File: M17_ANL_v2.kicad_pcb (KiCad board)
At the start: 2 copper layers, 63.9 x 19.6 mm, 108 parts, among them IC1 ADF7021, J1 USB_A, J2 RF_PORT, J3 Conn_01x05, J4 Conn_01x05, U1 STM32F303CBTx, U2 AP1117-33, X1 ASV-xxxMHz, X2 ASV-xxxMHz

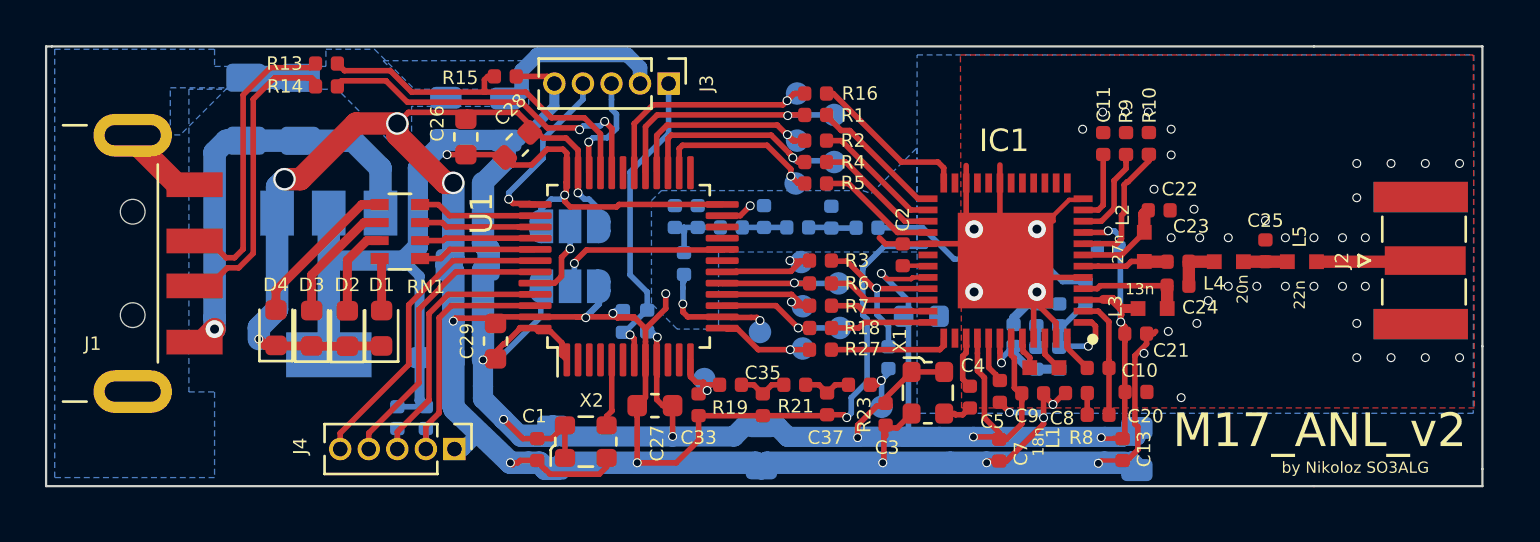
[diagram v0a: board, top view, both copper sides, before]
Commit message: added choke for radio part of M17_ANL_v2 added choke of input and output of the voltage regulator
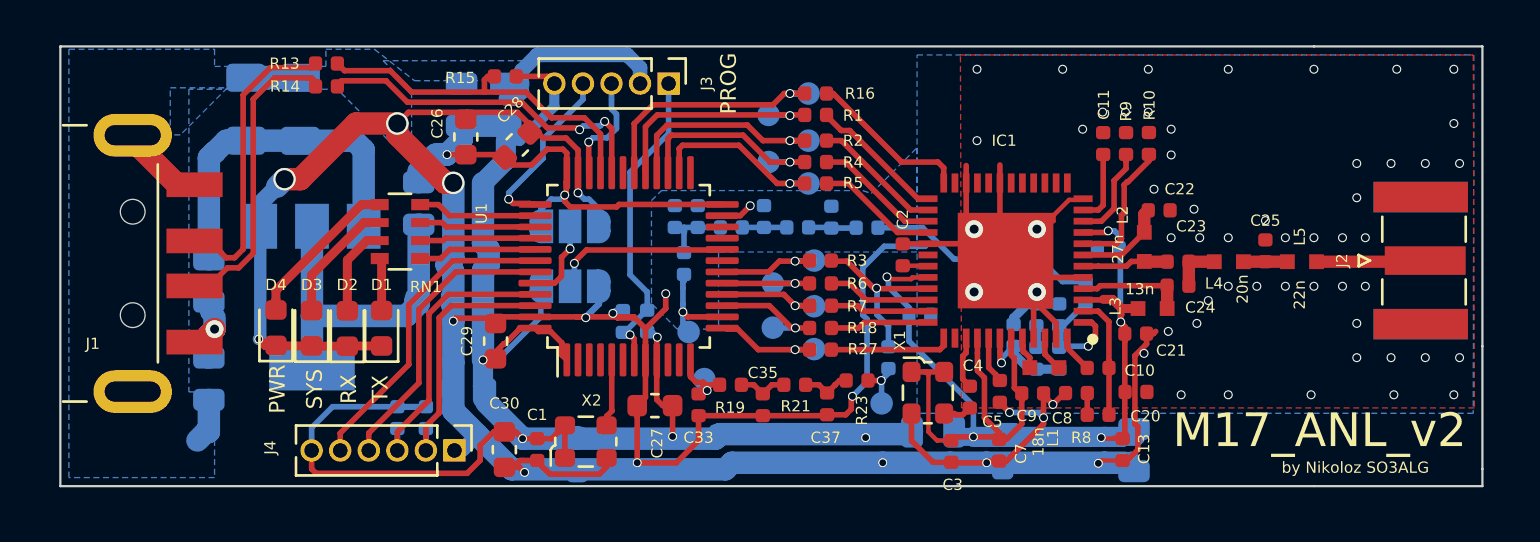
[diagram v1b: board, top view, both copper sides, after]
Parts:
- added C31: 10n, Capacitor_SMD:C_0402_1005Metric, B.Cu at (121.0, 98.2)
- added C44: 100n, Capacitor_SMD:C_0603_1608Metric, B.Cu at (99.4, 97.5)
- added C45: 100n, Capacitor_SMD:C_0805_2012Metric, B.Cu at (89.4, 101.0)
- added L6: 10uH, Inductor_SMD:L_0805_2012Metric, B.Cu at (98.7, 93.2)
- added L7: 1uH, Inductor_SMD:L_0805_2012Metric, B.Cu at (89.4, 96.6)
- added L8: 10uH, Inductor_SMD:L_0805_2012Metric, B.Cu at (121.6, 103.4)
- C30: moved to F.Cu
- C41, C42: value 10n -> 1n; footprint Capacitor_SMD:C_0805_2012Metric -> Capacitor_SMD:C_0603_1608Metric
- C43: value 10n -> 100n; footprint Capacitor_SMD:C_0805_2012Metric -> Capacitor_SMD:C_0603_1608Metric
- J3: value Conn_01x05 -> PROG
- J4: value Conn_01x05 -> Conn_01x06; footprint Connector_PinHeader_1.27mm:PinHeader_1x05_P1.27mm_Vertical -> Connector_PinHeader_1.27mm:PinHeader_1x06_P1.27mm_Vertical
- moved C31 16.5 mm to (105.8, 104.4), turned to 90 degrees
- moved C41 10.7 mm to (124.7, 104.3)
- moved C42 7.43 mm to (112.1, 104.3)
- moved C43 5.52 mm to (101.0, 101.5)
- moved C30 5.06 mm to (102.6, 104.2), turned to 90 degrees
- moved C3 3.36 mm to (122.4, 104.2)
- moved TP12 3.17 mm to (110.7, 98.9)
- moved TP9 2.98 mm to (114.5, 98.7)
- moved TP2 2.92 mm to (114.3, 91.4)
- moved TP4 2.92 mm to (114.3, 89.3)
- moved TP7 2.92 mm to (114.5, 96.8)
- moved U2 0.95 mm to (94.0, 97.4)
- moved C18 0.94 mm to (100.6, 88.8)
- moved C19 0.67 mm to (102.6, 88.8)
- moved TP8 0.58 mm to (116.3, 95.8)
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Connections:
- C1 pad 1: GND -> VCC_MCU
- C1 pad 2: MoDem_VCC -> GND
- C17 pad 1: VBUS -> Net-(C17-Pad1)
- C18 pad 1: MoDem_VCC -> VCC_MCU
- C19 pad 1: MoDem_VCC -> VCC_MCU
- C26 pad 2: MoDem_VCC -> VCC_MCU
- C27 pad 2: MoDem_VCC -> VCC_MCU
- C28 pad 1: MoDem_VCC -> VCC_MCU
- C29 pad 1: MoDem_VCC -> VCC_MCU
- C30 pad 2: MoDem_VCC -> VCC_MCU
- C31 pad 2: MoDem_VCC -> VCC_MCU
- C42 pad 1: MoDem_VCC -> VCC_MCU
- C43 pad 1: MoDem_VCC -> VCC_MCU
- C6 pad 1: VBUS -> Net-(C17-Pad1)
- J3 pad 5: MoDem_VCC -> VCC_MCU
- JP1 pad 1: MoDem_VCC -> VCC_MCU
- JP2 pad 1: MoDem_VCC -> VCC_MCU
- R15 pad 2: MoDem_VCC -> VCC_MCU
- R17 pad 2: MoDem_VCC -> VCC_MCU
- R28 pad 2: MoDem_VCC -> VCC_MCU
- R29 pad 2: MoDem_VCC -> VCC_MCU
- U1 pad 1: MoDem_VCC -> VCC_MCU
- U1 pad 24: MoDem_VCC -> VCC_MCU
- U1 pad 36: MoDem_VCC -> VCC_MCU
- U1 pad 48: MoDem_VCC -> VCC_MCU
- U1 pad 9: MoDem_VCC -> VCC_MCU
- U2 pad 2: MoDem_VCC -> Net-(C44-Pad1)
- U2 pad 3: VBUS -> Net-(C17-Pad1)
- X2 pad 1: MoDem_VCC -> VCC_MCU
- X2 pad 4: MoDem_VCC -> VCC_MCU
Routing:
- net MoDem_VCC: track 160.3 -> 53.8 mm, vias 12 -> 5
- net VCC_MCU: track 0.00 -> 102.3 mm, vias 0 -> 7
- net Net-(C17-Pad1): track 0.00 -> 15.3 mm
- net VBUS: track 19.1 -> 3.85 mm
- net Net-(C44-Pad1): track 0.00 -> 15.0 mm
- net GND: track 202.2 -> 205.7 mm, vias 60 -> 73
- net TxRx_Data: track 5.86 -> 4.88 mm
- net SPI_EN: track 11.5 -> 10.6 mm
- net DAC_OUT: track 5.79 -> 4.94 mm, vias 2 -> 1
- net SPI_MISO: track 10.4 -> 9.62 mm
- net RF_CLKOUT: track 6.03 -> 5.31 mm
- net SPI_MOSI: track 9.74 -> 9.14 mm
- net RF_EN: track 10.9 -> 11.4 mm
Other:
- board size 63.9 x 19.6 mm -> 63.2 x 19.6 mm
- board text added: "PWR"
- board text added: "RX"
- board text added: "SYS"
- board text added: "TX"

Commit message: Plotted new PDF of schematic
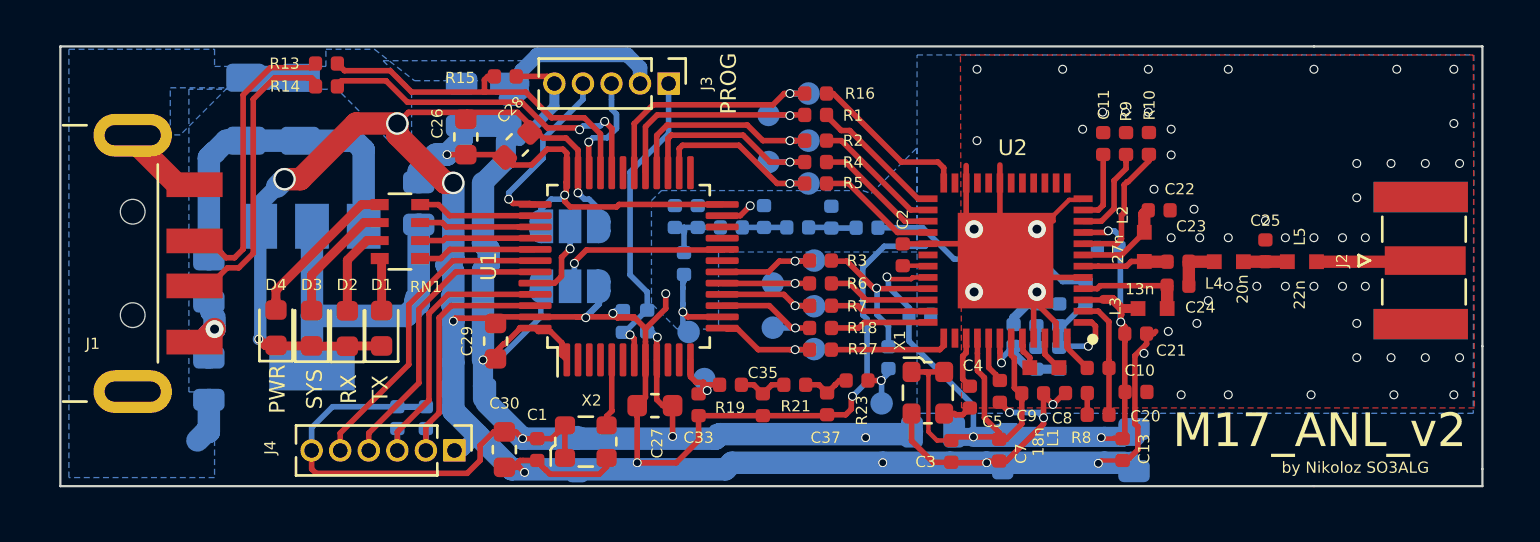
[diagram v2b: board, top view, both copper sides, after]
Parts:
- renumbered IC1 to U2, U2 to U3

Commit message: Readme header description added
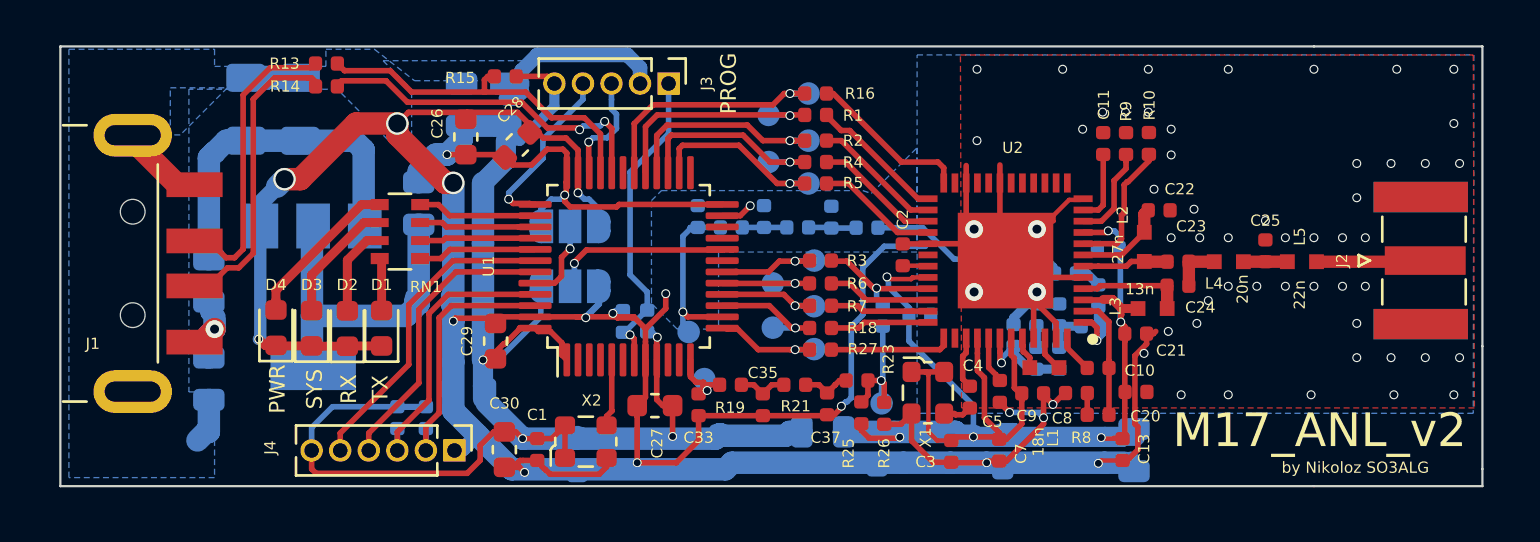
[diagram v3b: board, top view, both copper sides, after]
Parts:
- added C46: 1n, Capacitor_SMD:C_0603_1608Metric, B.Cu at (119.1, 104.1)
- added R31: 47k, Resistor_SMD:R_0402_1005Metric, B.Cu at (129.0, 97.3)
- added R32: 100, Resistor_SMD:R_0402_1005Metric, B.Cu at (128.7, 98.7)
- R24: value 1k -> 100k
- R25, R26: value ? -> 1k; moved to F.Cu
- moved R26 12.8 mm to (119.4, 102.6)
- moved R25 10.3 mm to (118.4, 102.5)
- moved L8 4.90 mm to (116.7, 103.4)
- moved C39 1.90 mm to (119.4, 98.2)
- moved C40 1.23 mm to (127.5, 96.3), turned to 180 degrees
- moved U3 0.05 mm to (94.0, 97.4)
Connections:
- C14 pad 1: VCO_IN -> Net-(C14-Pad1)
- C34 pad 2: Net-(C34-Pad2) -> DAC_OUT
- C40 pad 1: VCO_IN -> Net-(C40-Pad1)
- R11 pad 1: VCO_IN -> Net-(C14-Pad1)
- R20 pad 2: Net-(C34-Pad2) -> DAC_OUT
- R25 pad 1: Net-(C34-Pad2) -> FMDemod
- R25 pad 2: DAC_OUT -> MoDem_VCC
- R26 pad 1: Net-(C34-Pad2) -> GND
- R26 pad 2: GND -> FMDemod
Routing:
- net MoDem_VCC: track 53.8 -> 63.0 mm, vias 5 -> 6
- net VCC_MCU: track 102.3 -> 96.2 mm, vias 7 -> 6
- net FMDemod: track 2.43 -> 6.31 mm
- net DAC_OUT: track 4.94 -> 8.47 mm
- net Net-(C34-Pad2): track 3.18 -> 0.00 mm
- net Net-(C14-Pad1): track 0.00 -> 2.20 mm
- net VCO_IN: track 5.50 -> 3.31 mm
- net Net-(C39-Pad2): track 7.63 -> 5.67 mm
- net GND: track 205.7 -> 207.6 mm, vias 73 -> 72
- net FMMod: track 11.1 -> 9.74 mm
- net Net-(C40-Pad1): track 0.00 -> 1.19 mm
- net SPI_MOSI: track 9.14 -> 9.96 mm
